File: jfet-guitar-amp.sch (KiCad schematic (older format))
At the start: 51 parts, among them J1 Conn_2, J2 Conn_2, J3 Conn_3, Q1 J201, Q2 J201, Q3 J201, U1 4580, U2 TSX9291

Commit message: minor component value changes
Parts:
- C14, C15, C16, C2, C3: value 10u -> 4u7
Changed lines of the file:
@@
 EESchema Schematic File Version 4
+LIBS:jfet-guitar-amp-cache
 EELAYER 26 0
 EELAYER END
@@
 P 1675 1225
 F 0 "C3" H 1583 1179 50  0000 R CNN
-F 1 "10u" H 1583 1270 50  0000 R CNN
+F 1 "4u7" H 1583 1270 50  0000 R CNN
 F 2 "Capacitor_SMD:C_0805_2012Metric" H 1675 1225 50  0001 C CNN
 F 3 "~" H 1675 1225 50  0001 C CNN
@@
 P 1850 1225
 F 0 "C2" H 1758 1179 50  0000 R CNN
-F 1 "10u" H 1758 1270 50  0000 R CNN
+F 1 "4u7" H 1758 1270 50  0000 R CNN
 F 2 "Capacitor_SMD:C_0805_2012Metric" H 1850 1225 50  0001 C CNN
 F 3 "~" H 1850 1225 50  0001 C CNN
@@
 P 7175 4100
 F 0 "C16" H 7083 4054 50  0000 R CNN
-F 1 "10u" H 7083 4145 50  0000 R CNN
+F 1 "4u7" H 7083 4145 50  0000 R CNN
 F 2 "Capacitor_SMD:C_0805_2012Metric" H 7175 4100 50  0001 C CNN
 F 3 "~" H 7175 4100 50  0001 C CNN
@@
 P 7175 2800
 F 0 "C15" H 7083 2754 50  0000 R CNN
-F 1 "10u" H 7083 2845 50  0000 R CNN
+F 1 "4u7" H 7083 2845 50  0000 R CNN
 F 2 "Capacitor_SMD:C_0805_2012Metric" H 7175 2800 50  0001 C CNN
 F 3 "~" H 7175 2800 50  0001 C CNN
@@
 P 5850 4000
 F 0 "C14" H 5800 3925 50  0000 R CNN
-F 1 "10u" H 5800 4075 50  0000 R CNN
+F 1 "4u7" H 5800 4075 50  0000 R CNN
 F 2 "Capacitor_SMD:C_0805_2012Metric" H 5850 4000 50  0001 C CNN
 F 3 "~" H 5850 4000 50  0001 C CNN

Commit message: added PCB mount headphone socket, minor component changes
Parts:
- removed J3: Conn_3, Footprints:wire_strainrelief_3, symbol Connector:Conn_01x03_Female
- added J3: AudioJack4, Connector_Audio:Jack_3.5mm_PJ320D_Horizontal, symbol Connector:AudioJack4
- C2, C3: value 4u7 -> 10u; footprint Capacitor_SMD:C_0805_2012Metric -> Capacitor_SMD:C_1206_3216Metric
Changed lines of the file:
@@
 P 1675 1225
 F 0 "C3" H 1583 1179 50  0000 R CNN
-F 1 "4u7" H 1583 1270 50  0000 R CNN
-F 2 "Capacitor_SMD:C_0805_2012Metric" H 1675 1225 50  0001 C CNN
+F 1 "10u" H 1583 1270 50  0000 R CNN
+F 2 "Capacitor_SMD:C_1206_3216Metric" H 1675 1225 50  0001 C CNN
 F 3 "~" H 1675 1225 50  0001 C CNN
 	1    1675 1225
@@
 P 1850 1225
 F 0 "C2" H 1758 1179 50  0000 R CNN
-F 1 "4u7" H 1758 1270 50  0000 R CNN
-F 2 "Capacitor_SMD:C_0805_2012Metric" H 1850 1225 50  0001 C CNN
+F 1 "10u" H 1758 1270 50  0000 R CNN
+F 2 "Capacitor_SMD:C_1206_3216Metric" H 1850 1225 50  0001 C CNN
 F 3 "~" H 1850 1225 50  0001 C CNN
 	1    1850 1225
@@
 $EndComp
 $Comp
-L Connector:Conn_01x03_Female J3
-U 1 1 5C1085D3
-P 8975 3025
-F 0 "J3" H 8868 2700 50  0000 C CNN
-F 1 "Conn_3" H 8868 2791 50  0000 C CNN
-F 2 "Footprints:wire_strainrelief_3" H 8975 3025 50  0001 C CNN
-F 3 "~" H 8975 3025 50  0001 C CNN
-	1    8975 3025
-	1    0    0    1
-$EndComp
-$Comp
 L Amplifier_Operational:NE5532 U1
 U 2 1 5C07D10E
@@
 $EndComp
 Wire Wire Line
-	8775 3125 8700 3125
-Wire Wire Line
-	8700 3125 8700 3375
-Wire Wire Line
 	2275 3625 2425 3625
 Wire Wire Line
@@
 Wire Wire Line
 	4975 1200 5300 1200
+$Comp
+L Connector:AudioJack4 J3
+U 1 1 5C4D0C6D
+P 8975 3125
+F 0 "J3" H 8645 3008 50  0000 R CNN
+F 1 "AudioJack4" H 8645 3099 50  0000 R CNN
+F 2 "Connector_Audio:Jack_3.5mm_PJ320D_Horizontal" H 8975 3125 50  0001 C CNN
+F 3 "~" H 8975 3125 50  0001 C CNN
+	1    8975 3125
+	-1   0    0    1
+$EndComp
+Wire Wire Line
+	8775 3225 8700 3225
+Wire Wire Line
+	8700 3225 8700 3375
 $EndSCHEMATC

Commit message: prepare to send to manufacture
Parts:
- R21, R22: value 4K7 -> NF
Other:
- note added: "MMBF4117\nRs = 16K6ish\nRd = 100Kish"
- note removed: "MMBF411x?"
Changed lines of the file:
@@
 	2775 4150 3175 4150
 Connection ~ 3175 4150
-Text Notes 3025 4450 0    50   ~ 0
-MMBF411x?
+Text Notes 2925 4900 0    50   ~ 0
+MMBF4117\nRs = 16K6ish\nRd = 100Kish
 $Comp
 L Amplifier_Operational:MCP6001-OT U2
@@
 P 7250 950
 F 0 "R21" H 7192 904 50  0000 R CNN
-F 1 "4K7" H 7192 995 50  0000 R CNN
+F 1 "NF" H 7192 995 50  0000 R CNN
 F 2 "Resistor_SMD:R_0805_2012Metric" H 7250 950 50  0001 C CNN
 F 3 "~" H 7250 950 50  0001 C CNN
@@
 P 7250 1250
 F 0 "R22" H 7192 1204 50  0000 R CNN
-F 1 "4K7" H 7192 1295 50  0000 R CNN
+F 1 "NF" H 7192 1295 50  0000 R CNN
 F 2 "Resistor_SMD:R_0805_2012Metric" H 7250 1250 50  0001 C CNN
 F 3 "~" H 7250 1250 50  0001 C CNN

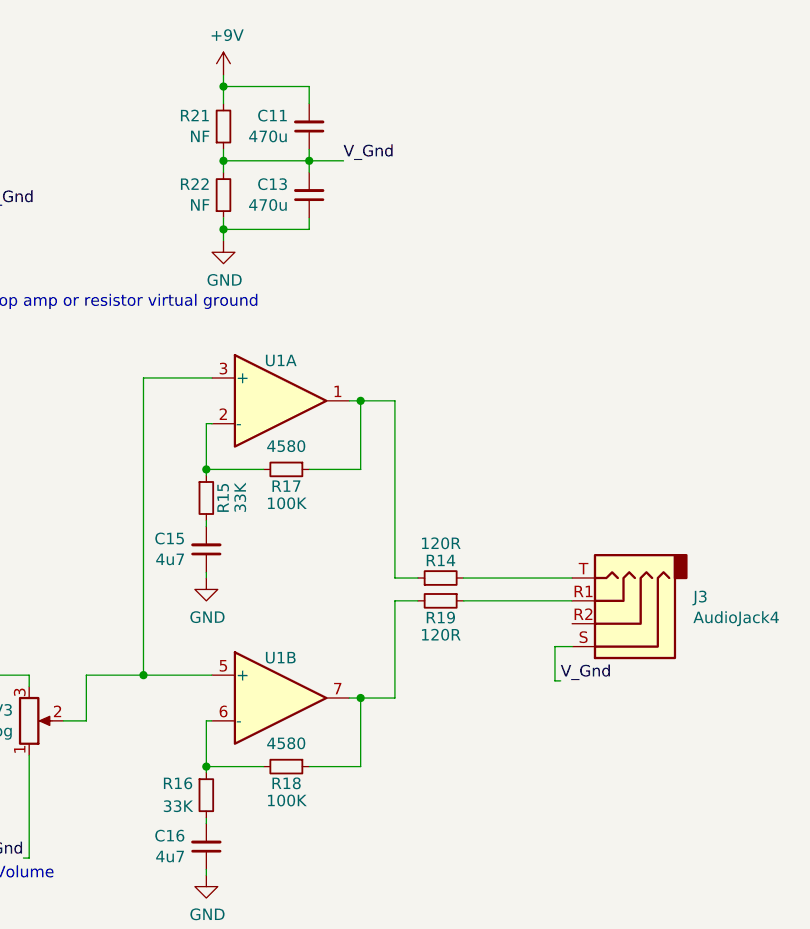
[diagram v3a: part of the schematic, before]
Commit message: minor schematic changes to feedback loop and BOM, tag for prototype production
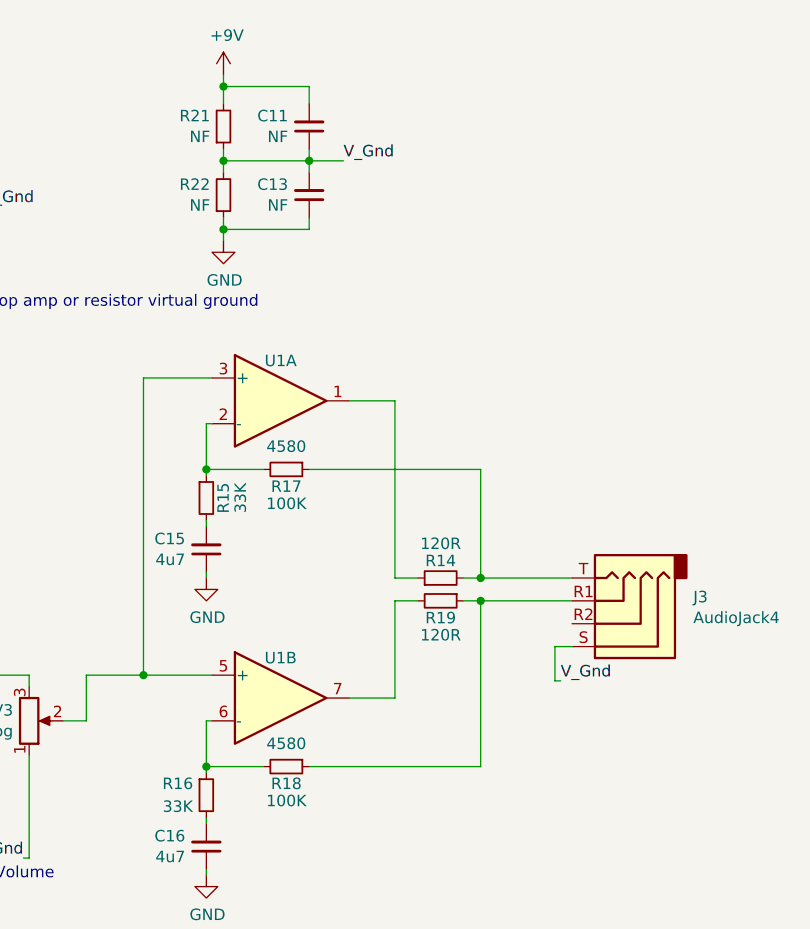
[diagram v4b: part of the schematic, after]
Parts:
- C11, C13: value 470u -> NF
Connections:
- net at R19.2, U1.7: no longer R18.1
- net at R14.1, U1.1: no longer R17.1
- net at J3.T, R14.2: now also R17.1
- net at J3.R1, R19.1: now also R18.1
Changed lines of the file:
@@
 Wire Wire Line
 	7175 3750 7175 3775
-Wire Wire Line
-	7625 3750 7850 3750
-Wire Wire Line
-	7850 3750 7850 3450
-Wire Wire Line
-	7850 3450 7800 3450
 $Comp
 L power:GND #PWR0102
@@
 Wire Wire Line
 	7175 2450 7175 2475
-Wire Wire Line
-	7625 2450 7850 2450
-Wire Wire Line
-	7850 2450 7850 2150
-Wire Wire Line
-	7850 2150 7800 2150
 $Comp
 L power:GND #PWR0103
@@
 	8000 2925 8000 2150
 Wire Wire Line
-	8000 2150 7850 2150
-Connection ~ 7850 2150
-Wire Wire Line
 	8100 3025 8000 3025
-Connection ~ 7850 3450
-Wire Wire Line
-	7850 3450 8000 3450
 Wire Wire Line
 	8000 3450 8000 3025
@@
 	2275 4150 2775 4150
 Wire Wire Line
-	8300 2925 8775 2925
-Wire Wire Line
-	8300 3025 8775 3025
+	8300 2925 8375 2925
+Wire Wire Line
+	8300 3025 8375 3025
 $Comp
 L Device:R_Small R14
@@
 P 7625 950
 F 0 "C11" H 7533 904 50  0000 R CNN
-F 1 "470u" H 7533 995 50  0000 R CNN
+F 1 "NF" H 7533 995 50  0000 R CNN
 F 2 "Capacitor_SMD:C_Elec_8x6.2" H 7625 950 50  0001 C CNN
 F 3 "~" H 7625 950 50  0001 C CNN
@@
 P 7625 1250
 F 0 "C13" H 7533 1204 50  0000 R CNN
-F 1 "470u" H 7533 1295 50  0000 R CNN
+F 1 "NF" H 7533 1295 50  0000 R CNN
 F 2 "Capacitor_SMD:C_Elec_8x6.2" H 7625 1250 50  0001 C CNN
 F 3 "~" H 7625 1250 50  0001 C CNN
@@
 Wire Wire Line
 	8700 3225 8700 3375
+Wire Wire Line
+	7800 3450 8000 3450
+Wire Wire Line
+	8375 3750 8375 3025
+Wire Wire Line
+	7625 3750 8375 3750
+Connection ~ 8375 3025
+Wire Wire Line
+	8375 3025 8775 3025
+Wire Wire Line
+	8375 2925 8375 2450
+Connection ~ 8375 2925
+Wire Wire Line
+	8375 2925 8775 2925
+Wire Wire Line
+	7625 2450 8375 2450
+Wire Wire Line
+	7800 2150 8000 2150
 $EndSCHEMATC

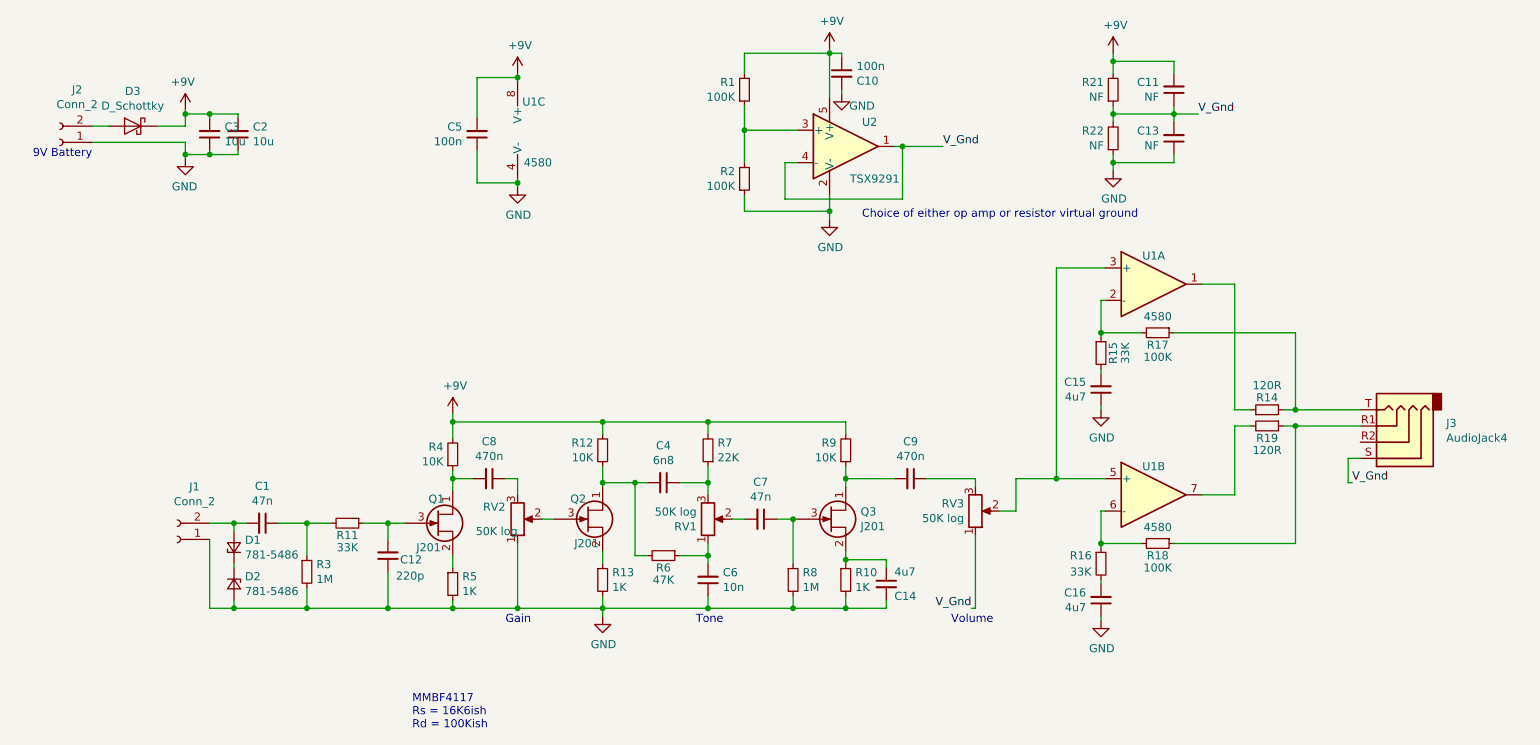
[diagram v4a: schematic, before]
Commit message: small tweaks: decoupling for split supply, tidied up schematic, moved via to reduce likelihood of ground loops
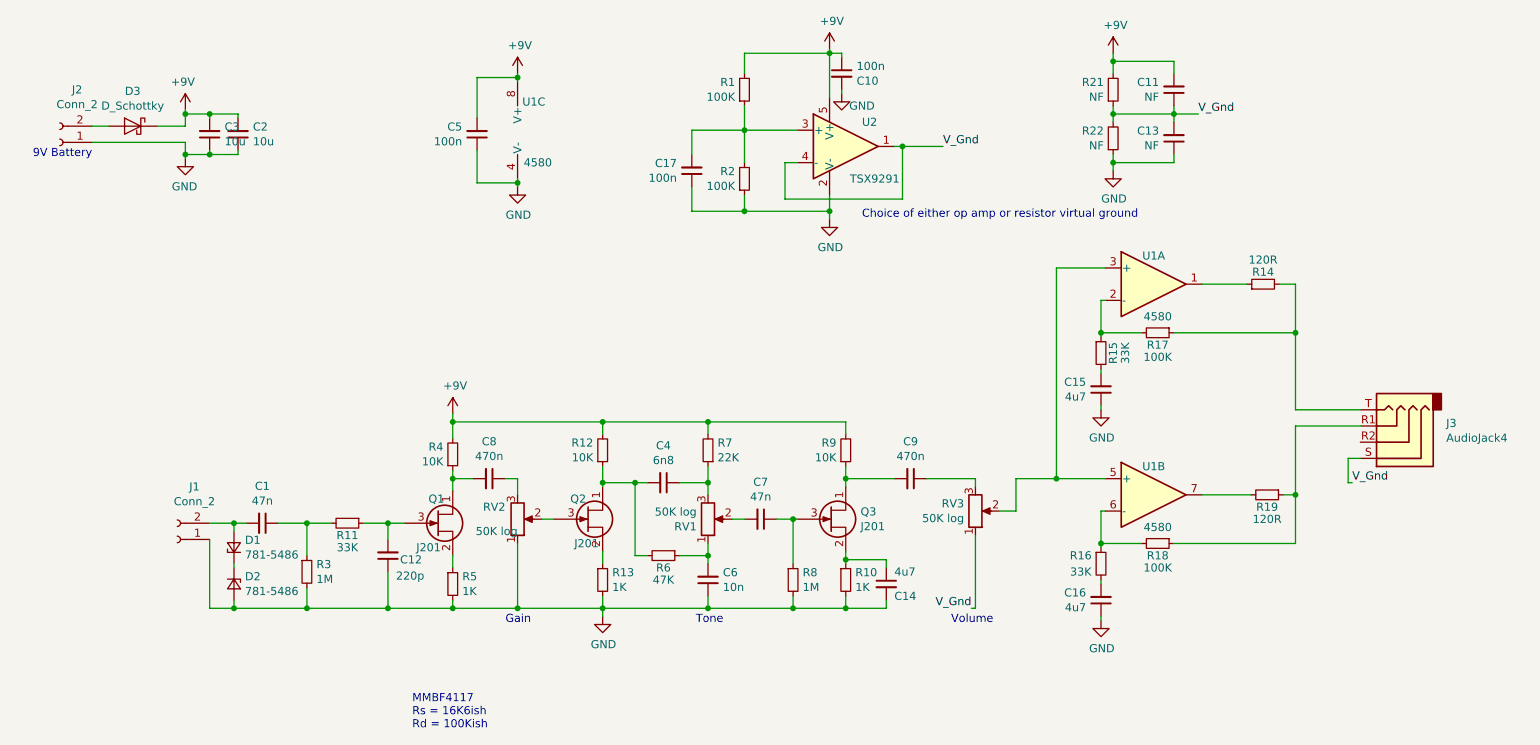
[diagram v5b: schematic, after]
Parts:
- added C17: 100n, Capacitor_SMD:C_0805_2012Metric, symbol Device:C_Small
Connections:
- net GND: now also C17.1
- net at R1.1, R2.2, U2.3 (+): now also C17.2
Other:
- moved on the sheet: R14, R19
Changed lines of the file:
@@
 EESchema Schematic File Version 4
 LIBS:jfet-guitar-amp-cache
-EELAYER 26 0
+EELAYER 29 0
 EELAYER END
 $Descr A4 11693 8268
@@
 Connection ~ 6900 3350
 Wire Wire Line
-	8100 2925 8000 2925
-Wire Wire Line
-	8000 2925 8000 2150
-Wire Wire Line
-	8100 3025 8000 3025
-Wire Wire Line
-	8000 3450 8000 3025
-Wire Wire Line
 	6900 2050 7200 2050
 Wire Wire Line
@@
 	2275 4150 2775 4150
 Wire Wire Line
-	8300 2925 8375 2925
-Wire Wire Line
-	8300 3025 8375 3025
+	8300 3450 8375 3450
 $Comp
 L Device:R_Small R14
 U 1 1 5C14A092
-P 8200 2925
-F 0 "R14" V 8275 2925 50  0000 C CNN
-F 1 "120R" V 8350 2925 50  0000 C CNN
-F 2 "Resistor_SMD:R_0805_2012Metric" H 8200 2925 50  0001 C CNN
-F 3 "~" H 8200 2925 50  0001 C CNN
-	1    8200 2925
+P 8175 2150
+F 0 "R14" V 8250 2150 50  0000 C CNN
+F 1 "120R" V 8325 2150 50  0000 C CNN
+F 2 "Resistor_SMD:R_0805_2012Metric" H 8175 2150 50  0001 C CNN
+F 3 "~" H 8175 2150 50  0001 C CNN
+	1    8175 2150
 	0    -1   -1   0
 $EndComp
@@
 L Device:R_Small R19
 U 1 1 5C14E7AA
-P 8200 3025
-F 0 "R19" V 8275 3025 50  0000 C CNN
-F 1 "120R" V 8350 3025 50  0000 C CNN
-F 2 "Resistor_SMD:R_0805_2012Metric" H 8200 3025 50  0001 C CNN
-F 3 "~" H 8200 3025 50  0001 C CNN
-	1    8200 3025
+P 8200 3450
+F 0 "R19" V 8275 3450 50  0000 C CNN
+F 1 "120R" V 8350 3450 50  0000 C CNN
+F 2 "Resistor_SMD:R_0805_2012Metric" H 8200 3450 50  0001 C CNN
+F 3 "~" H 8200 3450 50  0001 C CNN
+	1    8200 3450
 	0    1    1    0
 $EndComp
@@
 Wire Wire Line
 	4975 1200 5300 1200
+Wire Wire Line
+	8775 3225 8700 3225
+Wire Wire Line
+	8700 3225 8700 3375
+Wire Wire Line
+	8375 3750 8375 3450
+Wire Wire Line
+	7625 3750 8375 3750
+Connection ~ 8375 3450
+Wire Wire Line
+	8375 2925 8375 2450
+Wire Wire Line
+	8375 2925 8775 2925
+Wire Wire Line
+	7625 2450 8375 2450
+$Comp
+L Device:C_Small C17
+U 1 1 5C9EF1CE
+P 4650 1450
+F 0 "C17" H 4558 1404 50  0000 R CNN
+F 1 "100n" H 4558 1495 50  0000 R CNN
+F 2 "Capacitor_SMD:C_0805_2012Metric" H 4650 1450 50  0001 C CNN
+F 3 "~" H 4650 1450 50  0001 C CNN
+	1    4650 1450
+	1    0    0    1
+$EndComp
+Wire Wire Line
+	4975 1200 4650 1200
+Wire Wire Line
+	4650 1200 4650 1350
+Wire Wire Line
+	4650 1550 4650 1700
+Wire Wire Line
+	4650 1700 4975 1700
+Connection ~ 4975 1700
+Wire Wire Line
+	8275 2150 8375 2150
+Wire Wire Line
+	8375 2150 8375 2450
+Connection ~ 8375 2450
+Wire Wire Line
+	7800 2150 8075 2150
+Wire Wire Line
+	7800 3450 8100 3450
+Wire Wire Line
+	8775 3025 8375 3025
 $Comp
 L Connector:AudioJack4 J3
@@
 $EndComp
 Wire Wire Line
-	8775 3225 8700 3225
-Wire Wire Line
-	8700 3225 8700 3375
-Wire Wire Line
-	7800 3450 8000 3450
-Wire Wire Line
-	8375 3750 8375 3025
-Wire Wire Line
-	7625 3750 8375 3750
-Connection ~ 8375 3025
-Wire Wire Line
-	8375 3025 8775 3025
-Wire Wire Line
-	8375 2925 8375 2450
-Connection ~ 8375 2925
-Wire Wire Line
-	8375 2925 8775 2925
-Wire Wire Line
-	7625 2450 8375 2450
-Wire Wire Line
-	7800 2150 8000 2150
+	8375 3025 8375 3450
 $EndSCHEMATC
